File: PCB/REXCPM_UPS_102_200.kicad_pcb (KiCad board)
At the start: 2 copper layers, 52.1 x 16.1 mm, 7 parts, among them J2 Conn_01x03_Pin, J3 Conn_02x20_Odd_Even, U1 2G02

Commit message: fix 102_200 name
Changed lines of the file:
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@@
   (paper "USLetter")
   (title_block
-    (title "REXCPM UPS 102/200")
+    (title "REXCPM UPS 102_200")
     (date "2023-09-02")
     (rev "001")
@@
     (fp_arc (start 4.906989 3.352321) (mid 4.800001 2.952056) (end 4.905239 2.551328)
       (stroke (width 0.1) (type default)) (layer "F.SilkS"))
-    (fp_arc (start 5.3 1.697943) (mid 5.280925 1.852064) (end 5.224755 1.996844)
+    (fp_arc (start 5.3 1.697943) (mid 5.280926 1.852063) (end 5.224755 1.996844)
       (stroke (width 0.1) (type default)) (layer "F.SilkS"))
     (fp_line (start -6.35 -1.6375) (end -5.55 -1.6375)
@@
     (fp_arc (start 4.906989 3.352321) (mid 4.800001 2.952056) (end 4.905239 2.551328)
       (stroke (width 0.1) (type default)) (layer "F.SilkS"))
-    (fp_arc (start 5.3 1.697943) (mid 5.280878 1.85205) (end 5.224755 1.996844)
+    (fp_arc (start 5.3 1.697943) (mid 5.280878 1.852051) (end 5.224755 1.996844)
       (stroke (width 0.1) (type default)) (layer "F.SilkS"))
     (fp_line (start -6.35 -1.6375) (end -5.55 -1.6375)

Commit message: readme
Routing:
- net /BATT+: track 2.74 -> 32.7 mm
- net VBUS: track 31.6 -> 31.0 mm
- net GND: vias 3 -> 5

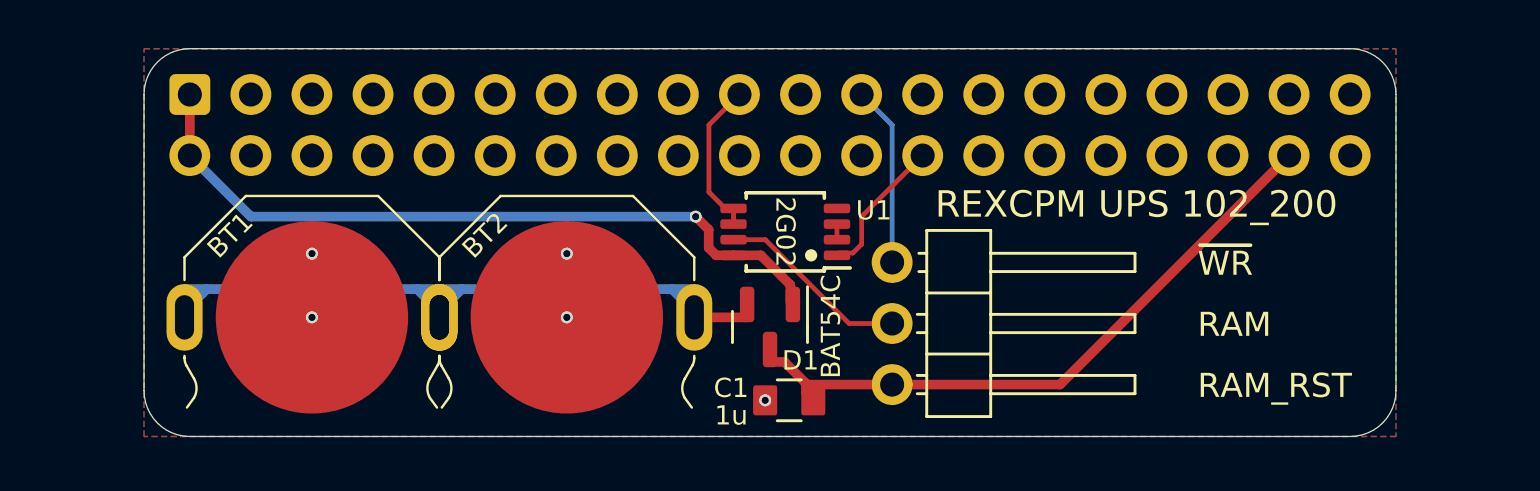
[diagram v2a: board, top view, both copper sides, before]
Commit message: 4-cells, add gnd wire, jst-sh connector
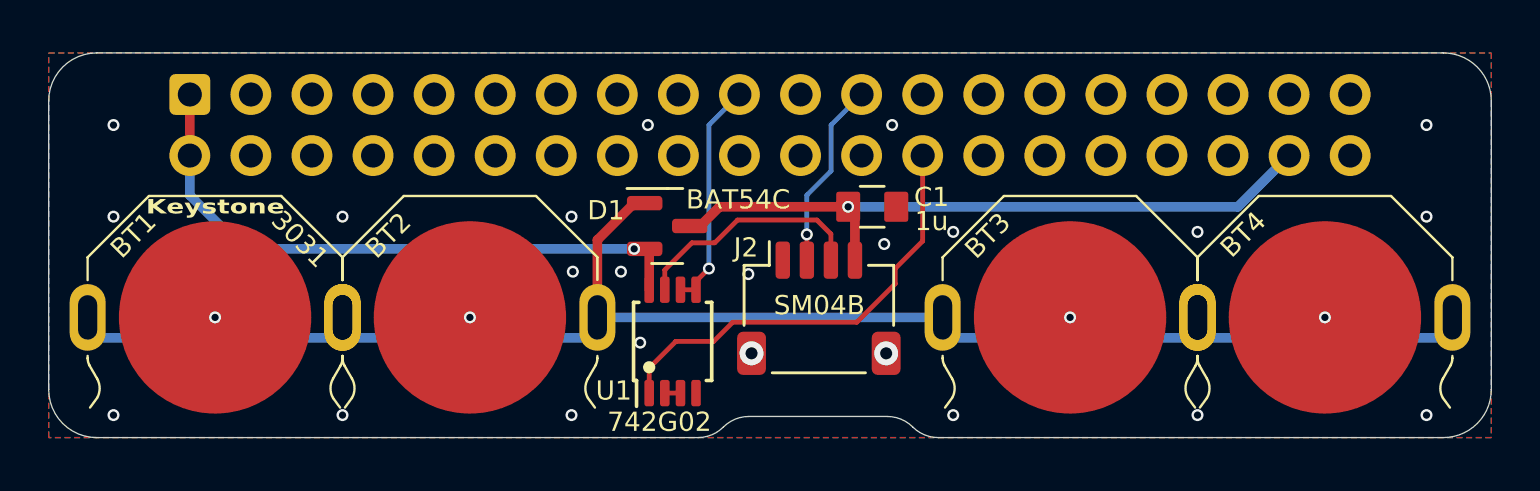
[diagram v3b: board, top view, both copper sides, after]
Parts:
- added BT3: Keystone_3031, 000_LOCAL:Keystone_3031, F.Cu at (149.0, 112.8)
- added BT4: Keystone_3031, 000_LOCAL:Keystone_3031, F.Cu at (159.6, 112.8)
- J2: value Conn_01x03_Pin -> SM04B; footprint 000_LOCAL:PinHeader_1x03_P2.54mm_Horizontal -> 000_LOCAL:JST_SH_SM04B-SRSS-TB_1x04-1MP_P1.00mm_Horizontal
- U1: value 2G02 -> 742G02
- moved C1 8.76 mm to (140.8, 108.2), turned to 0 degrees
- moved U1 6.53 mm to (132.5, 113.8), turned to 90 degrees
- moved D1 5.99 mm to (132.2, 109.0), turned to 0 degrees
- moved BT1 4.03 mm to (113.4, 112.8)
- moved BT2 4.03 mm to (124.0, 112.8)
- moved J2 3.59 mm to (138.6, 112.4)
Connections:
- D1 pad 1: VBUS -> /BATT+
- D1 pad 2: /BATT+ -> VBUS
- J2 pad 1: /~{WR} -> GND
- J2 pad 2: /RAM -> /~{WR}
- J2 pad 3: /RAM_RST -> /RAM
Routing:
- net /BATT+: track 32.7 -> 67.7 mm
- net /IO/~{M}: track 5.96 -> 18.5 mm
- net VBUS: track 31.0 -> 25.9 mm
- net /A15: track 6.55 -> 9.52 mm, vias 0 -> 1
- net /RAM: track 8.04 -> 9.92 mm
- net /RAM_RST: track 27.2 -> 28.5 mm, vias 0 -> 1
- net /~{WR}: track 7.51 -> 7.83 mm, vias 0 -> 1
- net GND: vias 5 -> 27
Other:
- board size 52.1 x 16.1 mm -> 60 x 16 mm
- board text added: "${COMMENT1}"
- board text added: "3031"
- board text added: "4321"
- board text added: "BATTERIES CR1025"
- board text added: "Keystone"
- board text added: "RAM_RST RAM ~{WR} GND"
- board text added: "UP"
- board text added: "v${REVISION}"
- board text removed: "${TITLE} - v${REVISION} ${COMMENT1}"
- board text removed: "RAM"
- board text removed: "RAM_RST"
- board text removed: "~{WR}"
